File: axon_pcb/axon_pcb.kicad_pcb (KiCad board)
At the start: 2 copper layers, 227.6 x 99.2 mm, 119 parts, among them J1 USB_C_Receptacle, J2 AVR_ISP Header, K1 KEYSW, K10 KEYSW, K11 KEYSW, K12 KEYSW, K13 KEYSW, K14 KEYSW, K15 KEYSW, K16 KEYSW, K17 KEYSW, K18 KEYSW, K19 KEYSW, K2 KEYSW, K20 KEYSW, K21 KEYSW, K22 KEYSW, K23 KEYSW, K24 KEYSW, K25 KEYSW, K26 KEYSW, K27 KEYSW, K28 KEYSW, K29 KEYSW, K3 KEYSW, K30 KEYSW, K31 KEYSW, K32 KEYSW, K33 KEYSW, K34 KEYSW, K35 KEYSW, K36 KEYSW, K37 KEYSW, K38 KEYSW, K39 KEYSW, K4 KEYSW, K40 KEYSW, K41 KEYSW, K42 KEYSW, K5 KEYSW, K6 KEYSW, K7 KEYSW, K8 KEYSW, K9 KEYSW, SW1 RESET, SW2 BOOT, U1 ATmega328P-PU, X1 16MHz

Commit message: added 7u support
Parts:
- added K43: KEYSW, keyswitches-daprice:SW_MX, F.Cu at (104.8, 57.1)
- added K44: KEYSW, keyswitches-daprice:SW_MX, F.Cu at (183.4, 57.1)
- added REF**: Stabilizer_MX_7u, personal:Stabilizer_MX_7u, F.Cu at (104.8, 57.1)
- G***: moved to B.Cu
- moved G*** 88.8 mm to (150.7, -24.6), turned to 180 degrees
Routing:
- net /col4: track 80.0 -> 96.6 mm
- net Net-(D37-Pad2): track 182.4 -> 199.0 mm
- net Net-(D40-Pad2): track 78.5 -> 83.2 mm
- net /col9: track 150.5 -> 152.8 mm
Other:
- board text added: "Inspired by Gingham Designed by Robin L. Toronto, CA. 2021"
- board text added: "SPACE-7u"
- board text removed: "Designed by Robin L. Toronto, CA. 2021"
- board text removed: "Inspired by Gingham"

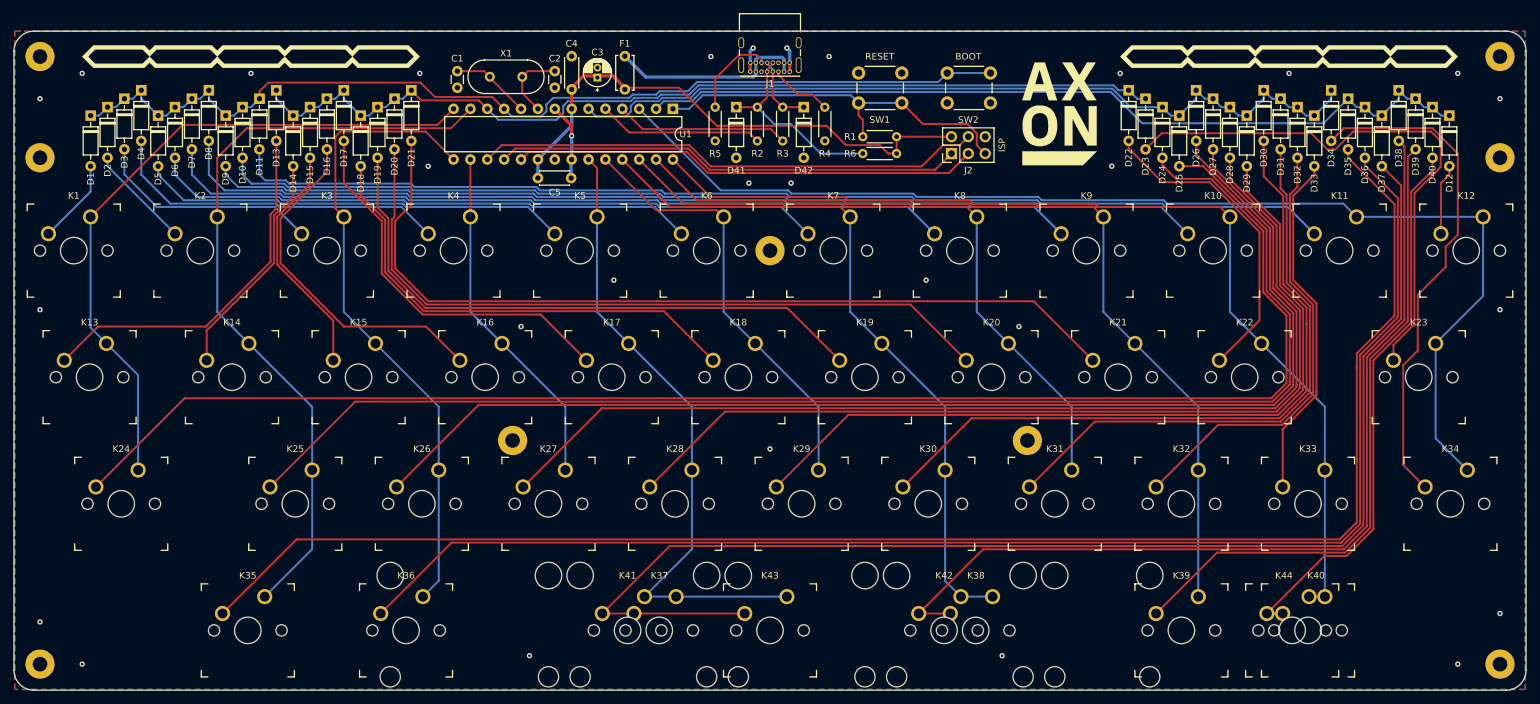
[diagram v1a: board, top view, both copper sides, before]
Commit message: adjusted footprints, added 6.25u support
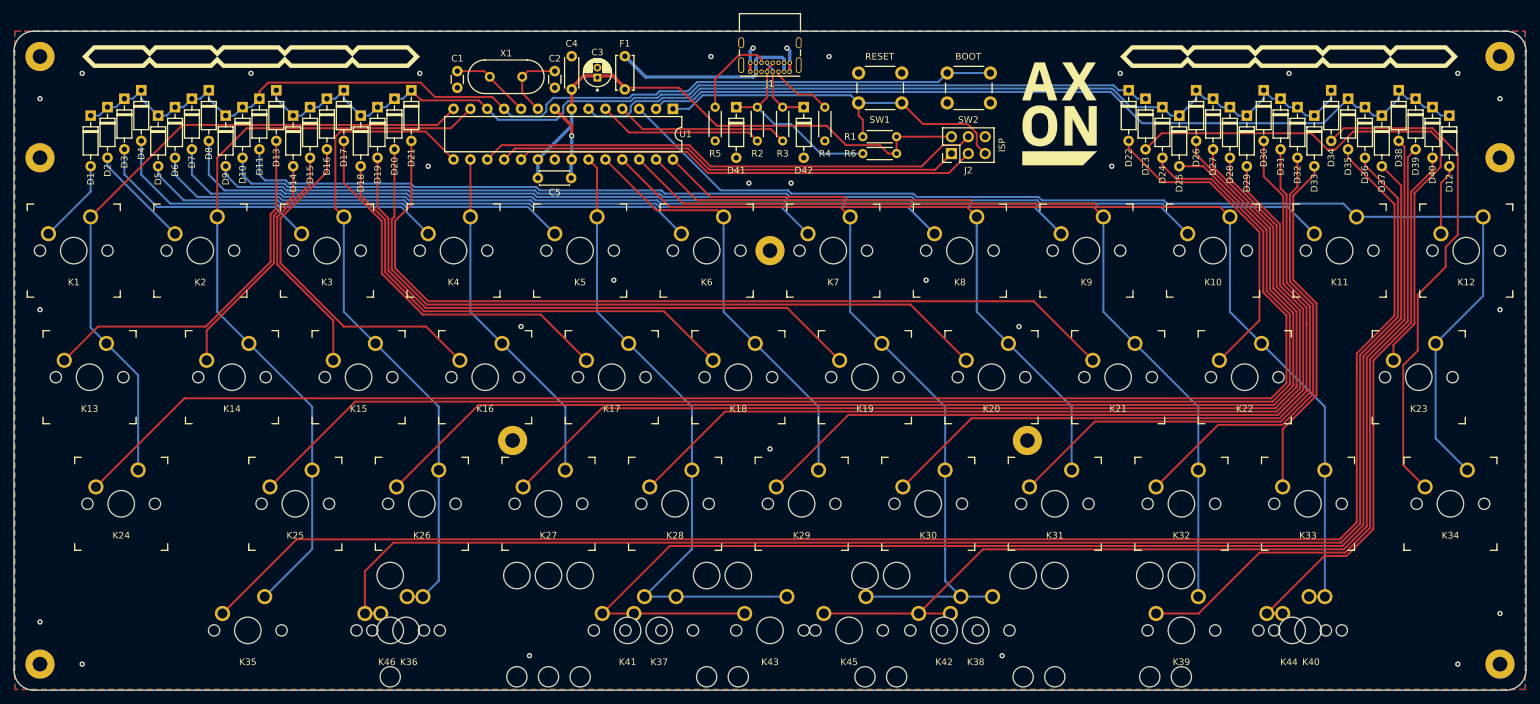
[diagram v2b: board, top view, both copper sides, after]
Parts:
- added K45: KEYSW, personal:SW_MX_Minimal_InsideSilkRef, F.Cu at (116.7, 57.1)
- added K46: KEYSW, personal:SW_MX_Minimal_InsideSilkRef, F.Cu at (47.6, 57.1)
- added REF**: Stabilizer_MX_6.25u, personal:Stabilizer_MX_6.25u, F.Cu at (116.7, 57.1)
- K1, K10, K11, K12, K13, K14, K15, K16, K17, K18, K19, K2, K20, K21, K22, K23, K24, K25, K26, K27, K28, K29, K3, K30, K31, K32, K33, K34, K4, K5, K6, K7, K8, K9: footprint keyswitches-daprice:SW_MX -> personal:SW_MX_InsideSilkRef
- K35, K36, K37, K38, K39, K40, K41, K42, K43, K44: footprint keyswitches-daprice:SW_MX -> personal:SW_MX_Minimal_InsideSilkRef
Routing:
- net Net-(D38-Pad2): track 138.3 -> 152.6 mm
- net /col6: track 106.7 -> 121.0 mm
- net Net-(D36-Pad2): track 212.4 -> 220.9 mm
- net /col2: track 96.5 -> 98.9 mm
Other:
- board text added: "SPACE 6.25u"
- board text added: "SPACE 7u"
- board text removed: "SPACE-7u"

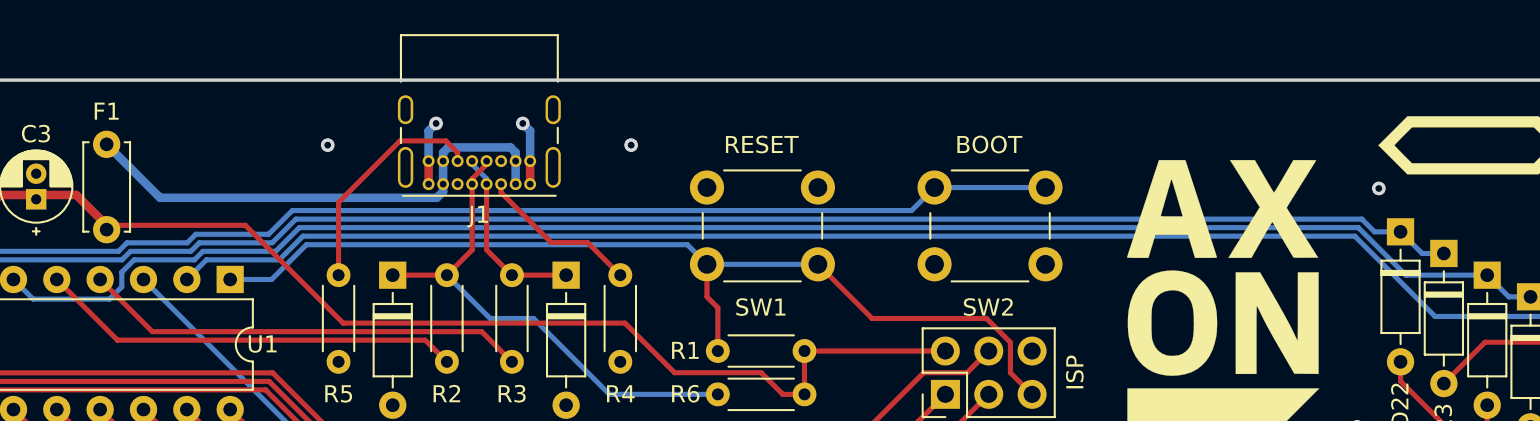
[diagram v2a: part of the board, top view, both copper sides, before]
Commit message: updated usb4085 footprint for easier handsoldering, added spacebar notes to schema
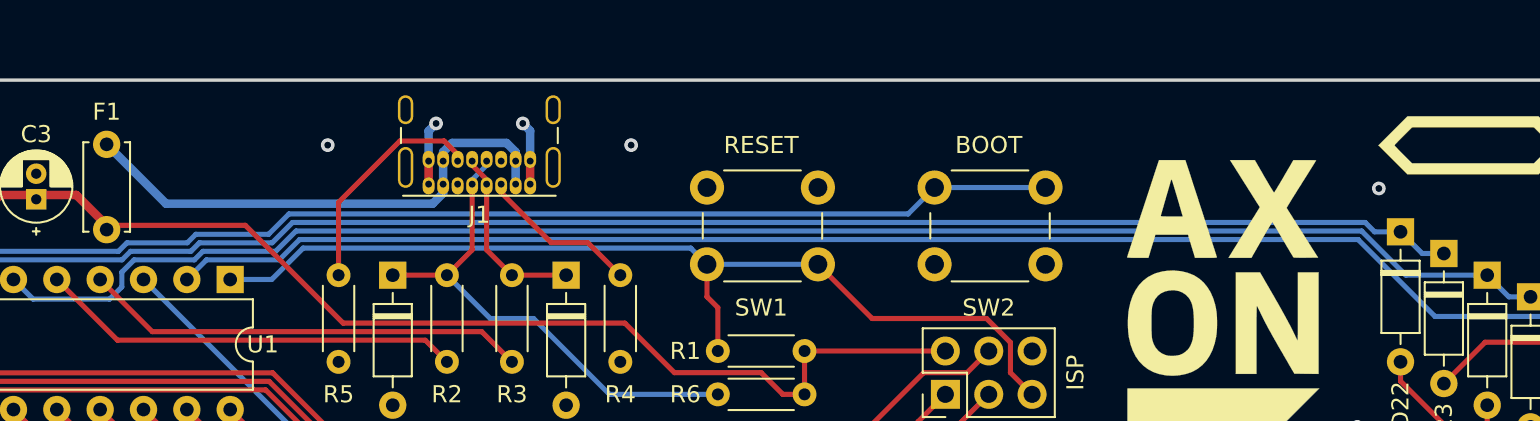
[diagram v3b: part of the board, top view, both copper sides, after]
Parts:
- J1: footprint Connector_USB:USB_C_Receptacle_GCT_USB4085 -> personal:USB_C_Receptacle_GCT_USB4085_personalized
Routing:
- net Net-(F1-Pad1): track 29.8 -> 30.4 mm

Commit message: minor routing and position adjustments
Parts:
- moved SW1 0.64 mm to (125.2, -22.2)
- moved R1 0.63 mm to (119.4, -17.1)
- moved R6 0.63 mm to (124.5, -14.6)

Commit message: minor edits
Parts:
- moved C5 0.13 mm to (69.8, -10.8)
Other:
- board text added: "2.25u"
- board text added: "2.75u"
- board text added: "6.25u"
- board text added: "7u"
- board text removed: "SPACE"
- board text removed: "SPACE 6.25u"
- board text removed: "SPACE 7u"
- board text removed: "SUPER"
